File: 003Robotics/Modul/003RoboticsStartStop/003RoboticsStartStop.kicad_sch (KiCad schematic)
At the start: 15 parts, among them J1 Conn_ARM_SWD_TagConnect_TC203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, J2 I/O Header, U2 TSOP392, U3 STM32C011F4, U4 LDK220PU33R

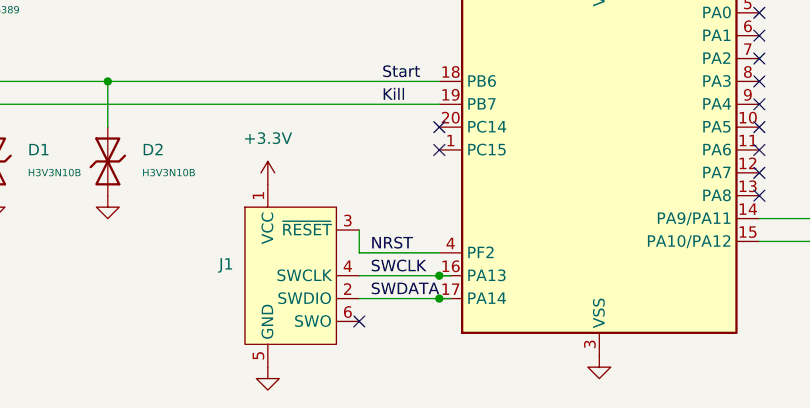
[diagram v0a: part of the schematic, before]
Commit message: Inverted SWDIO/SWCLK to correct pins.
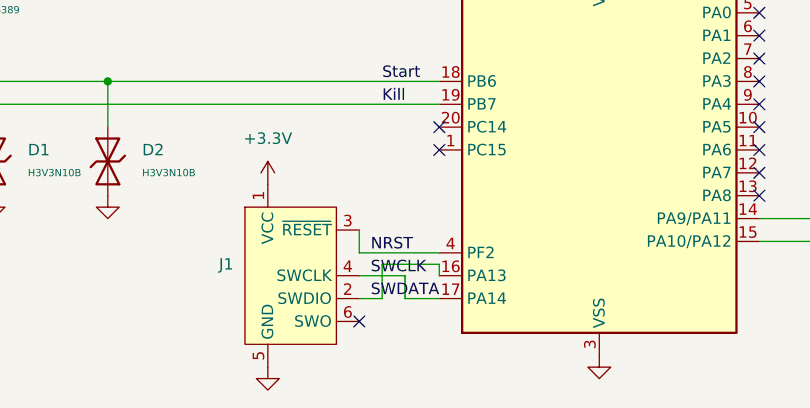
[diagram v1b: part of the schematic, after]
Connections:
- net SWCLK: now also U3.17 (PA14); no longer U3.16 (PA13)
- net SWDATA: now also U3.16 (PA13); no longer U3.17 (PA14)
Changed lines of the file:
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@@
-	)
-	(junction
-		(at 105.41 80.01)
-		(diameter 0)
-		(color 0 0 0 0)
 	)
 	(junction
@@
 	)
 	(junction
-		(at 105.41 82.55)
-		(diameter 0)
-		(color 0 0 0 0)
-	)
-	(junction
 		(at 168.91 73.66)
 		(diameter 0)
@@
 	(wire
 		(pts
+			(xy 101.6 80.01) (xy 101.6 82.55)
+		)
+		(stroke
+			(width 0)
+			(type default)
+		)
+	)
+	(wire
+		(pts
 			(xy 52.07 34.29) (xy 52.07 38.1)
 		)
@@
 	(wire
 		(pts
+			(xy 96.52 82.55) (xy 99.06 82.55)
+		)
+		(stroke
+			(width 0)
+			(type default)
+		)
+	)
+	(wire
+		(pts
 			(xy 168.91 44.45) (xy 168.91 48.26)
 		)
@@
 	(wire
 		(pts
-			(xy 105.41 82.55) (xy 106.68 82.55)
-		)
-		(stroke
-			(width 0)
-			(type default)
-		)
-	)
-	(wire
-		(pts
 			(xy 52.07 55.88) (xy 45.72 55.88)
 		)
@@
 	(wire
 		(pts
-			(xy 96.52 82.55) (xy 105.41 82.55)
-		)
-		(stroke
-			(width 0)
-			(type default)
-		)
-	)
-	(wire
-		(pts
 			(xy 45.72 58.42) (xy 68.58 58.42)
 		)
@@
 	(wire
 		(pts
+			(xy 96.52 80.01) (xy 101.6 80.01)
+		)
+		(stroke
+			(width 0)
+			(type default)
+		)
+	)
+	(wire
+		(pts
 			(xy 59.69 34.29) (xy 59.69 35.56)
 		)
@@
 	(wire
 		(pts
-			(xy 96.52 80.01) (xy 105.41 80.01)
+			(xy 99.06 82.55) (xy 99.06 78.74)
+		)
+		(stroke
+			(width 0)
+			(type default)
+		)
+	)
+	(wire
+		(pts
+			(xy 99.06 78.74) (xy 105.41 78.74)
 		)
 		(stroke
@@
 	(wire
 		(pts
-			(xy 105.41 80.01) (xy 106.68 80.01)
+			(xy 105.41 78.74) (xy 105.41 80.01)
 		)
 		(stroke
@@
 		)
 		(stroke
+			(width 0)
+			(type default)
+		)
+	)
+	(wire
+		(pts
+			(xy 101.6 82.55) (xy 105.41 82.55)
+		)
+		(stroke
